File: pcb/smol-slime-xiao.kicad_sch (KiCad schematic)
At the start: 11 parts, among them J1 Conn_01x02, U1 ICM-45686, U3 1532H, U4 XIAO-nRF52840-SMD

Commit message: Add MCU connectors
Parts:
- added J2: Conn_01x02, symbol Connector_Generic:Conn_01x02
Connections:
- net +5V: now also J2.1 (Pin_1)
- net GND: now also J2.2 (Pin_2)
- net VBAT: now reaches J1.2 (Pin_2), U4.15 (BAT)
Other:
- moved on the sheet: C3, J1, R1, R2, U2

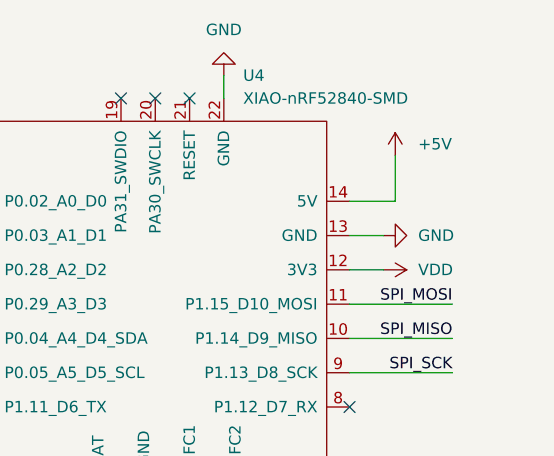
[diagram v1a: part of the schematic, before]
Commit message: Fix edge cuts
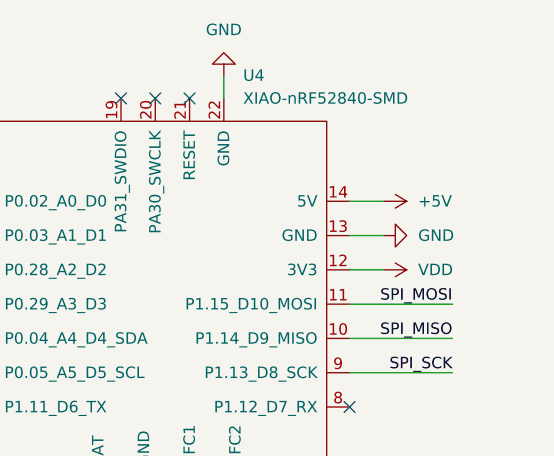
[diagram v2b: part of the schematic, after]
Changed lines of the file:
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@@
-	(wire
-		(pts
-			(xy 264.16 35.56) (xy 264.16 40.64)
-		)
-		(stroke
-			(width 0)
-			(type default)
-		)
-	)
 	(wire
 		(pts
@@
 	(wire
 		(pts
-			(xy 264.16 40.64) (xy 259.08 40.64)
+			(xy 262.89 40.64) (xy 259.08 40.64)
 		)
 		(stroke
@@
 	(symbol
 		(lib_id "power:+5V")
-		(at 264.16 35.56 0)
+		(at 262.89 40.64 270)
 		(unit 1)
 		(exclude_from_sim no)
@@
 		(fields_autoplaced yes)
 		(property "Reference" "#PWR017"
-			(at 264.16 39.37 0)
+			(at 259.08 40.64 0)
 			(effects
 				(font
@@
 		)
 		(property "Value" "+5V"
-			(at 266.7 34.2899 0)
+			(at 266.7 40.6399 90)
 			(effects
 				(font
@@
 		)
 		(property "Footprint" ""
-			(at 264.16 35.56 0)
+			(at 262.89 40.64 0)
 			(effects
 				(font
@@
 		)
 		(property "Datasheet" ""
-			(at 264.16 35.56 0)
+			(at 262.89 40.64 0)
 			(effects
 				(font
@@
 		)
 		(property "Description" "Power symbol creates a global label with name \"+5V\""
-			(at 264.16 35.56 0)
-			(effects
-				(font
+			(at 262.89 40.64 0)
+			(effects
+				(font

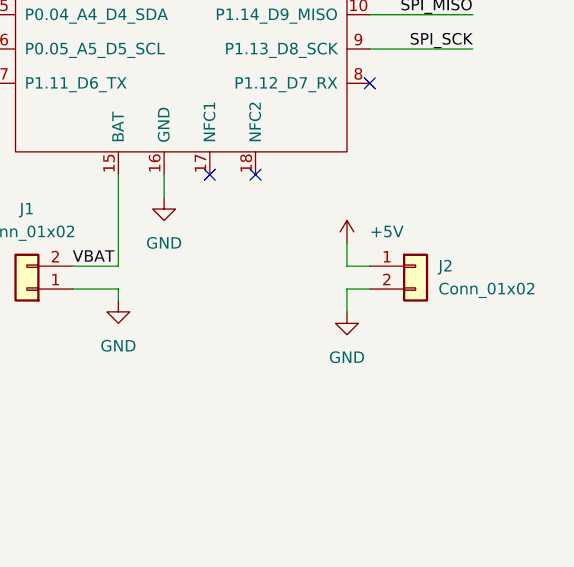
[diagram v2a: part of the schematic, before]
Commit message: Homogenise connector terminals
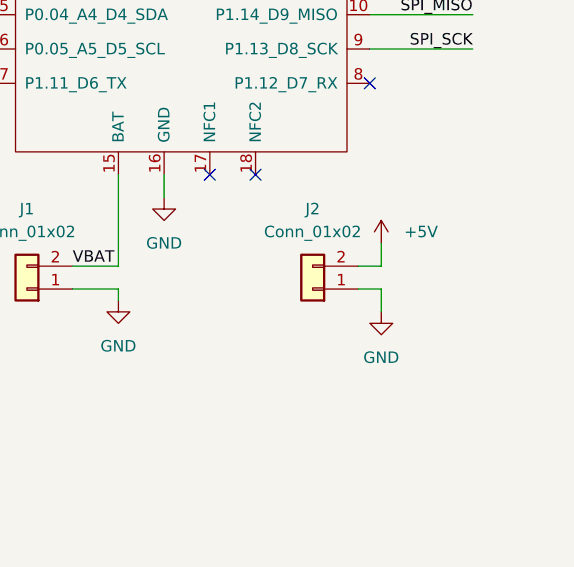
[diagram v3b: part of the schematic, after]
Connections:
- net +5V: now also J2.2 (Pin_2); no longer J2.1 (Pin_1)
- net GND: now also J2.1 (Pin_1); no longer J2.2 (Pin_2)
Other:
- moved on the sheet: J2
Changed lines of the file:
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@@
+	(wire
+		(pts
+			(xy 260.35 83.82) (xy 260.35 81.28)
+		)
+		(stroke
+			(width 0)
+			(type default)
+		)
+	)
 	(wire
 		(pts
@@
 	(wire
 		(pts
+			(xy 257.81 83.82) (xy 260.35 83.82)
+		)
+		(stroke
+			(width 0)
+			(type default)
+		)
+	)
+	(wire
+		(pts
 			(xy 154.94 138.43) (xy 154.94 140.97)
 		)
@@
 	(wire
 		(pts
-			(xy 256.54 86.36) (xy 256.54 88.9)
-		)
-		(stroke
-			(width 0)
-			(type default)
-		)
-	)
-	(wire
-		(pts
 			(xy 204.47 48.26) (xy 217.17 48.26)
 		)
@@
 	(wire
 		(pts
-			(xy 259.08 86.36) (xy 256.54 86.36)
-		)
-		(stroke
-			(width 0)
-			(type default)
-		)
-	)
-	(wire
-		(pts
 			(xy 262.89 40.64) (xy 259.08 40.64)
 		)
@@
 	(wire
 		(pts
-			(xy 259.08 83.82) (xy 256.54 83.82)
-		)
-		(stroke
-			(width 0)
-			(type default)
-		)
-	)
-	(wire
-		(pts
 			(xy 259.08 48.26) (xy 262.89 48.26)
 		)
@@
 	(wire
 		(pts
-			(xy 256.54 83.82) (xy 256.54 81.28)
-		)
-		(stroke
-			(width 0)
-			(type default)
-		)
-	)
-	(wire
-		(pts
 			(xy 231.14 73.66) (xy 231.14 83.82)
 		)
@@
 	(wire
 		(pts
+			(xy 257.81 86.36) (xy 260.35 86.36)
+		)
+		(stroke
+			(width 0)
+			(type default)
+		)
+	)
+	(wire
+		(pts
 			(xy 226.06 86.36) (xy 231.14 86.36)
+		)
+		(stroke
+			(width 0)
+			(type default)
+		)
+	)
+	(wire
+		(pts
+			(xy 260.35 86.36) (xy 260.35 88.9)
 		)
 		(stroke
@@
 	(symbol
 		(lib_id "power:GND")
-		(at 256.54 88.9 0)
+		(at 260.35 88.9 0)
 		(unit 1)
 		(exclude_from_sim no)
@@
 		(fields_autoplaced yes)
 		(property "Reference" "#PWR021"
-			(at 256.54 95.25 0)
+			(at 260.35 95.25 0)
 			(effects
 				(font
@@
 		)
 		(property "Value" "GND"
-			(at 256.54 93.98 0)
+			(at 260.35 93.98 0)
 			(effects
 				(font
@@
 		)
 		(property "Footprint" ""
-			(at 256.54 88.9 0)
+			(at 260.35 88.9 0)
 			(effects
 				(font
@@
 		)
 		(property "Datasheet" ""
-			(at 256.54 88.9 0)
+			(at 260.35 88.9 0)
 			(effects
 				(font
@@
 		)
 		(property "Description" "Power symbol creates a global label with name \"GND\" , ground"
-			(at 256.54 88.9 0)
+			(at 260.35 88.9 0)
 			(effects
 				(font
@@
 	(symbol
 		(lib_id "power:+5V")
-		(at 256.54 81.28 0)
+		(at 260.35 81.28 0)
 		(unit 1)
 		(exclude_from_sim no)
@@
 		(fields_autoplaced yes)
 		(property "Reference" "#PWR020"
-			(at 256.54 85.09 0)
+			(at 260.35 85.09 0)
 			(effects
 				(font
@@
 		)
 		(property "Value" "+5V"
-			(at 259.08 80.0099 0)
+			(at 262.89 80.0099 0)
 			(effects
 				(font
@@
 		)
 		(property "Footprint" ""
-			(at 256.54 81.28 0)
+			(at 260.35 81.28 0)
 			(effects
 				(font
@@
 		)
 		(property "Datasheet" ""
-			(at 256.54 81.28 0)
+			(at 260.35 81.28 0)
 			(effects
 				(font
@@
 		)
 		(property "Description" "Power symbol creates a global label with name \"+5V\""
-			(at 256.54 81.28 0)
+			(at 260.35 81.28 0)
 			(effects
 				(font
@@
 	(symbol
 		(lib_id "Connector_Generic:Conn_01x02")
-		(at 264.16 83.82 0)
+		(at 252.73 86.36 180)
 		(unit 1)
 		(exclude_from_sim no)
@@
 		(fields_autoplaced yes)
 		(property "Reference" "J2"
-			(at 266.7 83.8199 0)
-			(effects
-				(font
-					(size 1.27 1.27)
-				)
-				(justify left)
+			(at 252.73 77.47 0)
+			(effects
+				(font
+					(size 1.27 1.27)
+				)
 			)
 		)
 		(property "Value" "Conn_01x02"
-			(at 266.7 86.3599 0)
-			(effects
-				(font
-					(size 1.27 1.27)
-				)
-				(justify left)
+			(at 252.73 80.01 0)
+			(effects
+				(font
+					(size 1.27 1.27)
+				)
 			)
 		)
 		(property "Footprint" ""
-			(at 264.16 83.82 0)
+			(at 252.73 86.36 0)
 			(effects
 				(font
@@
 		)
 		(property "Datasheet" "~"
-			(at 264.16 83.82 0)
+			(at 252.73 86.36 0)
 			(effects
 				(font
@@
 		)
 		(property "Description" "Generic connector, single row, 01x02, script generated (kicad-library-utils/schlib/autogen/connector/)"
-			(at 264.16 83.82 0)
-			(effects
-				(font
+			(at 252.73 86.36 0)
+			(effects
+				(font

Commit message: Add pad to power connector
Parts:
- J2: footprint (none) -> Generic:PinPads_1x02_P2.54mm
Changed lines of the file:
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@@
 			)
 		)
-		(property "Footprint" ""
+		(property "Footprint" "Generic:PinPads_1x02_P2.54mm"
 			(at 252.73 86.36 0)
 			(effects

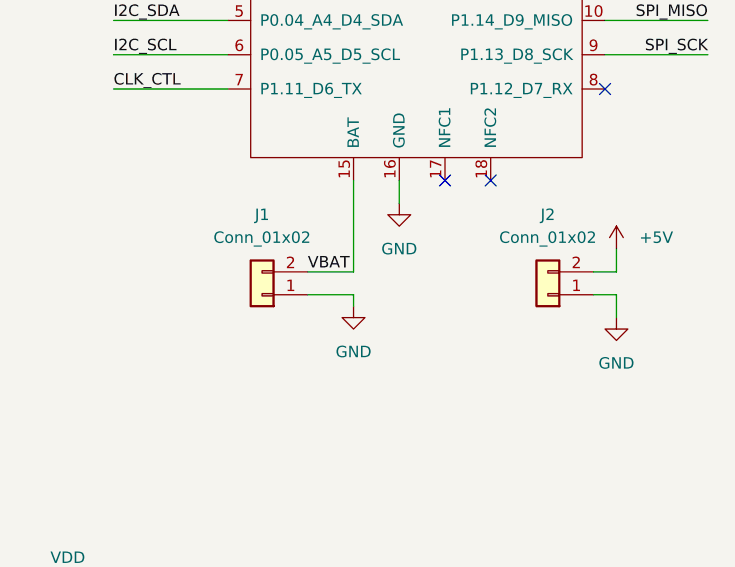
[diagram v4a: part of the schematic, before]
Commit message: Add battery JST connector
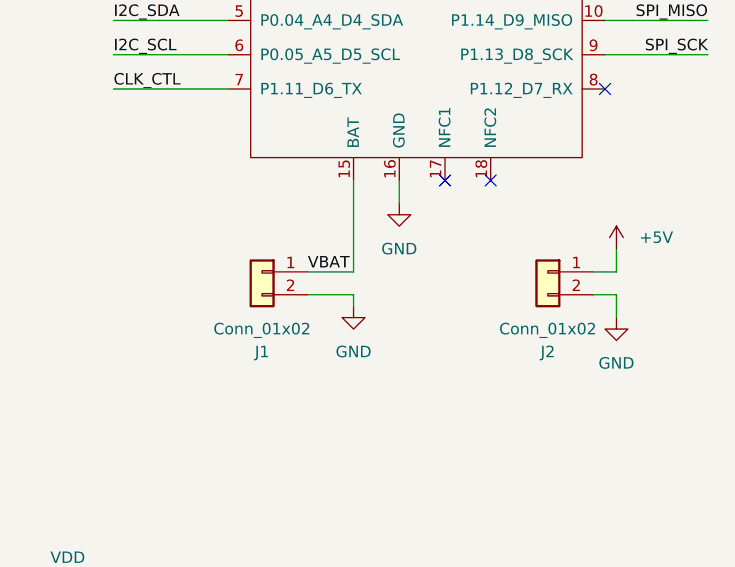
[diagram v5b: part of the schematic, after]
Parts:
- J1: footprint (none) -> Connector_JST:JST_PH_S2B-PH-K_1x02_P2.00mm_Horizontal
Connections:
- net +5V: now also J2.1 (Pin_1); no longer J2.2 (Pin_2)
- net GND: now also J1.2 (Pin_2), J2.2 (Pin_2); no longer J1.1 (Pin_1), J2.1 (Pin_1)
- net VBAT: now also J1.1 (Pin_1); no longer J1.2 (Pin_2)
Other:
- moved on the sheet: J1, J2
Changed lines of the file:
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@@
+	(wire
+		(pts
+			(xy 226.06 86.36) (xy 231.14 86.36)
+		)
+		(stroke
+			(width 0)
+			(type default)
+		)
+	)
 	(wire
 		(pts
@@
 	(wire
 		(pts
+			(xy 260.35 86.36) (xy 260.35 88.9)
+		)
+		(stroke
+			(width 0)
+			(type default)
+		)
+	)
+	(wire
+		(pts
 			(xy 257.81 86.36) (xy 260.35 86.36)
-		)
-		(stroke
-			(width 0)
-			(type default)
-		)
-	)
-	(wire
-		(pts
-			(xy 226.06 86.36) (xy 231.14 86.36)
-		)
-		(stroke
-			(width 0)
-			(type default)
-		)
-	)
-	(wire
-		(pts
-			(xy 260.35 86.36) (xy 260.35 88.9)
 		)
 		(stroke
@@
 	(symbol
 		(lib_id "Connector_Generic:Conn_01x02")
-		(at 220.98 86.36 180)
-		(unit 1)
-		(exclude_from_sim no)
-		(in_bom yes)
-		(on_board yes)
-		(dnp no)
-		(fields_autoplaced yes)
+		(at 220.98 83.82 0)
+		(mirror y)
+		(unit 1)
+		(exclude_from_sim no)
+		(in_bom yes)
+		(on_board yes)
+		(dnp no)
 		(property "Reference" "J1"
-			(at 220.98 77.47 0)
+			(at 220.98 92.71 0)
 			(effects
 				(font
@@
 		)
 		(property "Value" "Conn_01x02"
-			(at 220.98 80.01 0)
-			(effects
-				(font
-					(size 1.27 1.27)
-				)
-			)
-		)
-		(property "Footprint" ""
-			(at 220.98 86.36 0)
+			(at 220.98 90.17 0)
+			(effects
+				(font
+					(size 1.27 1.27)
+				)
+			)
+		)
+		(property "Footprint" "Connector_JST:JST_PH_S2B-PH-K_1x02_P2.00mm_Horizontal"
+			(at 220.98 83.82 0)
 			(effects
 				(font
@@
 		)
 		(property "Datasheet" "~"
-			(at 220.98 86.36 0)
+			(at 220.98 83.82 0)
 			(effects
 				(font
@@
 		)
 		(property "Description" "Generic connector, single row, 01x02, script generated (kicad-library-utils/schlib/autogen/connector/)"
-			(at 220.98 86.36 0)
+			(at 220.98 83.82 0)
 			(effects
 				(font
@@
 	(symbol
 		(lib_id "Connector_Generic:Conn_01x02")
-		(at 252.73 86.36 180)
-		(unit 1)
-		(exclude_from_sim no)
-		(in_bom yes)
-		(on_board yes)
-		(dnp no)
-		(fields_autoplaced yes)
+		(at 252.73 83.82 0)
+		(mirror y)
+		(unit 1)
+		(exclude_from_sim no)
+		(in_bom yes)
+		(on_board yes)
+		(dnp no)
 		(property "Reference" "J2"
-			(at 252.73 77.47 0)
+			(at 252.73 92.71 0)
 			(effects
 				(font
@@
 		)
 		(property "Value" "Conn_01x02"
-			(at 252.73 80.01 0)
+			(at 252.73 90.17 0)
 			(effects
 				(font
@@
 		)
 		(property "Footprint" "Generic:PinPads_1x02_P2.54mm"
-			(at 252.73 86.36 0)
+			(at 252.73 83.82 0)
 			(effects
 				(font
@@
 		)
 		(property "Datasheet" "~"
-			(at 252.73 86.36 0)
+			(at 252.73 83.82 0)
 			(effects
 				(font
@@
 		)
 		(property "Description" "Generic connector, single row, 01x02, script generated (kicad-library-utils/schlib/autogen/connector/)"
-			(at 252.73 86.36 0)
-			(effects
-				(font
+			(at 252.73 83.82 0)
+			(effects
+				(font

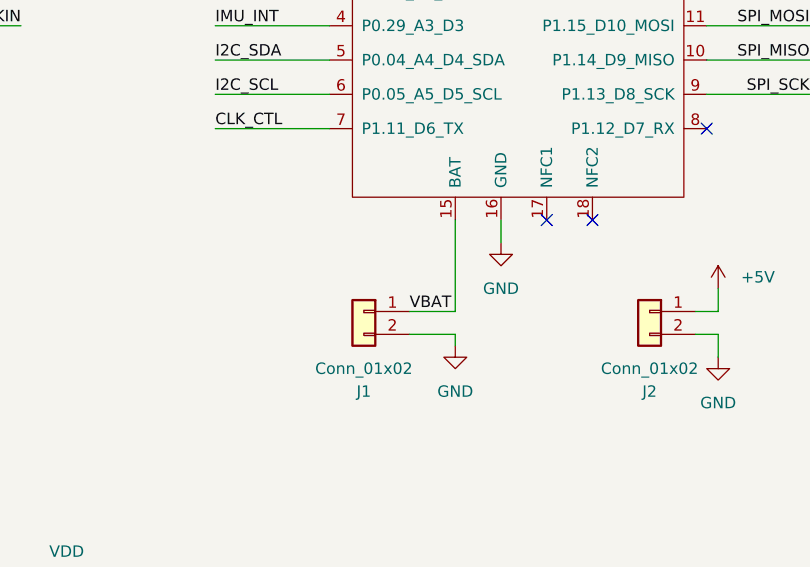
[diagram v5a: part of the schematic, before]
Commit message: Changed JST to SMT
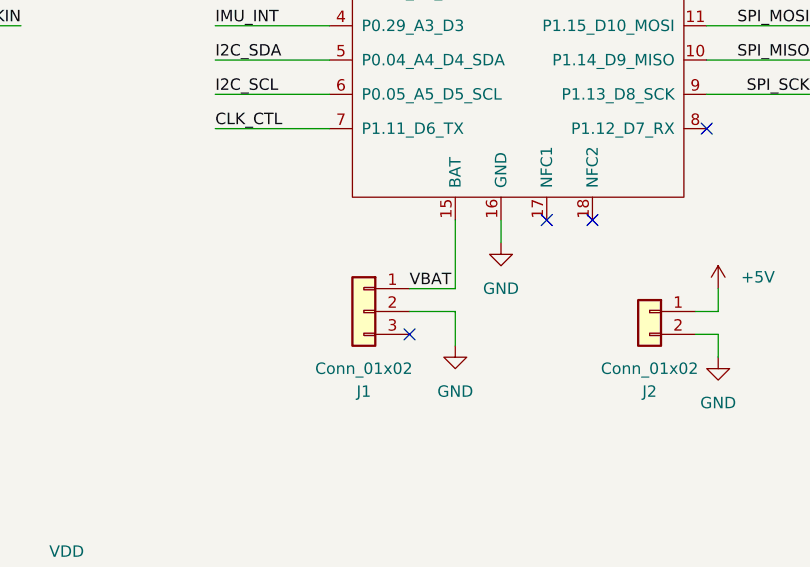
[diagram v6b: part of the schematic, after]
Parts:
- J1: footprint Connector_JST:JST_PH_S2B-PH-K_1x02_P2.00mm_Horizontal -> Generic:JST_PH2_SMT; symbol Connector_Generic:Conn_01x02 -> Connector_Generic:Conn_01x03
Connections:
- no-connect marks 13 -> 14
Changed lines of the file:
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@@
+	)
+	(no_connect
+		(at 226.06 86.36)
 	)
 	(no_connect
@@
 	(wire
 		(pts
+			(xy 231.14 83.82) (xy 231.14 87.63)
+		)
+		(stroke
+			(width 0)
+			(type default)
+		)
+	)
+	(wire
+		(pts
 			(xy 69.85 127) (xy 74.93 127)
 		)
@@
 	(wire
 		(pts
-			(xy 226.06 86.36) (xy 231.14 86.36)
+			(xy 231.14 83.82) (xy 226.06 83.82)
 		)
 		(stroke
@@
 	(wire
 		(pts
-			(xy 231.14 86.36) (xy 231.14 87.63)
-		)
-		(stroke
-			(width 0)
-			(type default)
-		)
-	)
-	(wire
-		(pts
-			(xy 231.14 73.66) (xy 231.14 83.82)
+			(xy 231.14 73.66) (xy 231.14 81.28)
 		)
 		(stroke
@@
 	(wire
 		(pts
-			(xy 226.06 83.82) (xy 231.14 83.82)
+			(xy 226.06 81.28) (xy 231.14 81.28)
 		)
 		(stroke
@@
 	)
 	(label "VBAT"
-		(at 226.06 83.82 0)
+		(at 226.06 81.28 0)
 		(effects
 			(font
@@
 	)
 	(symbol
-		(lib_id "Connector_Generic:Conn_01x02")
+		(lib_id "Connector_Generic:Conn_01x03")
 		(at 220.98 83.82 0)
 		(mirror y)
@@
 			)
 		)
-		(property "Footprint" "Connector_JST:JST_PH_S2B-PH-K_1x02_P2.00mm_Horizontal"
+		(property "Footprint" "Generic:JST_PH2_SMT"
 			(at 220.98 83.82 0)
 			(effects
@@
 			)
 		)
-		(property "Description" "Generic connector, single row, 01x02, script generated (kicad-library-utils/schlib/autogen/connector/)"
+		(property "Description" "Generic connector, single row, 01x03, script generated (kicad-library-utils/schlib/autogen/connector/)"
 			(at 220.98 83.82 0)
 			(effects
@@
 		(pin "1"
 		)
+		(pin "3"
+		)
 		(instances

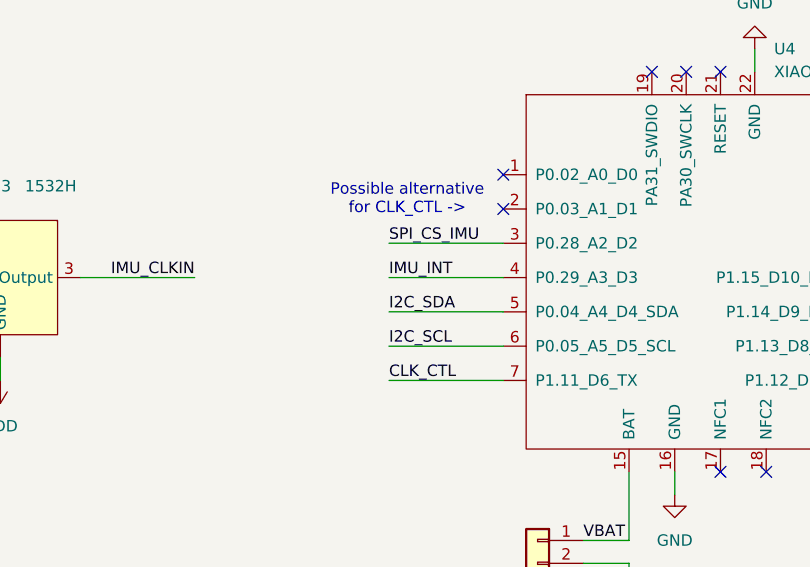
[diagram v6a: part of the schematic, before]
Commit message: Move CLK_CTL to alternate GPIO
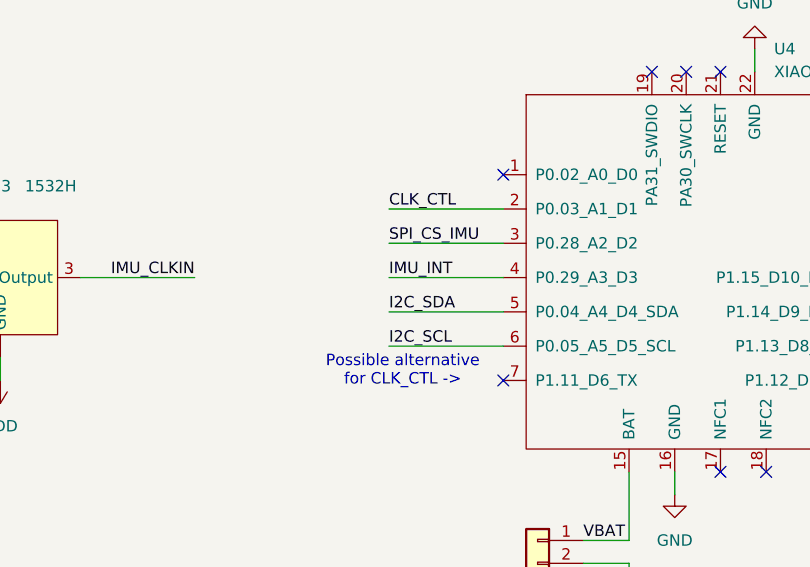
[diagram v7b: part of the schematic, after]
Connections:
- net CLK_CTL: now also U4.2 (P0.03_A1_D1); no longer U4.7 (P1.11_D6_TX)
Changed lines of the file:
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@@
 	(text "Possible alternative\nfor CLK_CTL ->"
 		(exclude_from_sim no)
-		(at 206.502 43.434 0)
+		(at 205.994 62.484 0)
 		(effects
 			(font
@@
 	)
 	(no_connect
-		(at 217.17 44.45)
-	)
-	(no_connect
 		(at 226.06 86.36)
 	)
@@
 	)
 	(no_connect
+		(at 217.17 63.5)
+	)
+	(no_connect
 		(at 233.68 29.21)
 	)
@@
 	(wire
 		(pts
-			(xy 204.47 63.5) (xy 217.17 63.5)
-		)
-		(stroke
-			(width 0)
-			(type default)
-		)
-	)
-	(wire
-		(pts
 			(xy 187.96 128.27) (xy 196.85 128.27)
 		)
@@
 		(pts
 			(xy 96.52 30.48) (xy 85.09 30.48)
+		)
+		(stroke
+			(width 0)
+			(type default)
+		)
+	)
+	(wire
+		(pts
+			(xy 204.47 44.45) (xy 217.17 44.45)
 		)
 		(stroke
@@
 	)
 	(label "CLK_CTL"
-		(at 204.47 63.5 0)
-		(effects
-			(font
+		(at 204.47 44.45 0)
+		(effects
+			(font

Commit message: Fix XIAO silkscreen overlap
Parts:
- U4: footprint Seeed Studio XIAO Series Library:XIAO-nRF52840-SMD -> Seeed Studio XIAO Series Library:XIAO-nRF52840-SMD-FixedSilkscreen
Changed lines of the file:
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@@
 			)
 		)
-		(property "Footprint" "Seeed Studio XIAO Series Library:XIAO-nRF52840-SMD"
+		(property "Footprint" "Seeed Studio XIAO Series Library:XIAO-nRF52840-SMD-FixedSilkscreen"
 			(at 229.87 46.99 0)
 			(effects
